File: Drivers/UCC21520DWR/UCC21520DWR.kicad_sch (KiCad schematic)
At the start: 21 parts, among them J1 Output, J3 Input, U1 UCC21520DWR

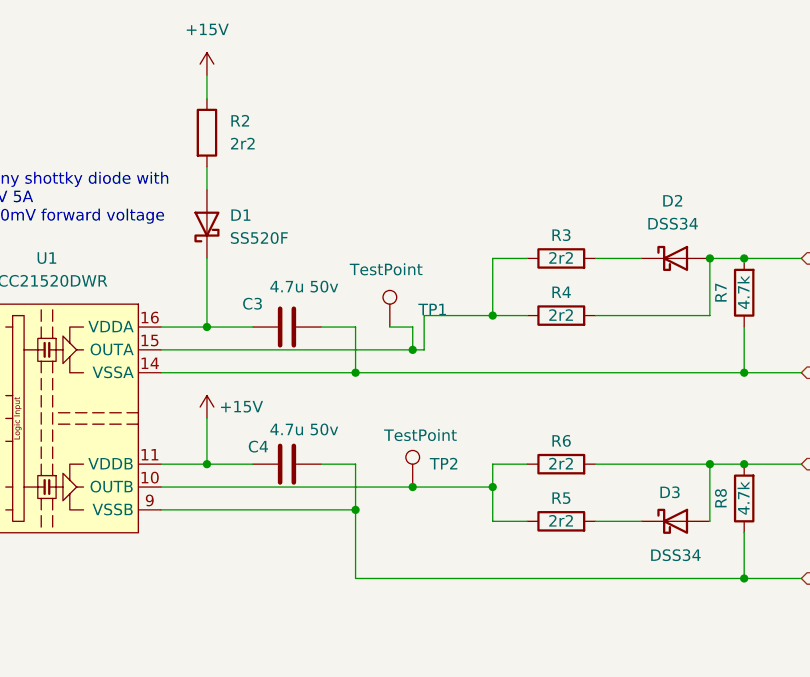
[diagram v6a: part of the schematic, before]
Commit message: fixes to caps and resistors on UCC21520DWR
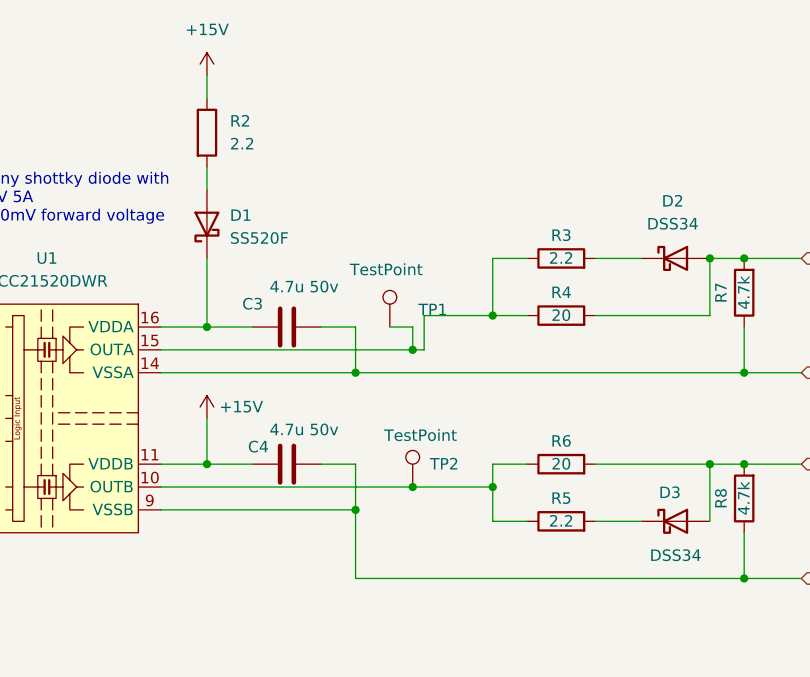
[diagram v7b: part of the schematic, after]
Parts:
- R2, R3, R5: value 2r2 -> 2.2
- R4, R6: value 2r2 -> 20; MPN C17521 -> C17544
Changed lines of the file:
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@@
       (effects (font (size 1.27 1.27)))
     )
-    (property "Value" "2r2" (at 196.85 90.17 90)
+    (property "Value" "20" (at 196.85 90.17 90)
       (effects (font (size 1.27 1.27)))
     )
@@
       (effects (font (size 1.27 1.27)) hide)
     )
-    (property "MPN" "C17521" (at 196.85 90.17 0)
+    (property "MPN" "C17544" (at 196.85 90.17 0)
       (effects (font (size 1.27 1.27)) hide)
     )
@@
       (effects (font (size 1.27 1.27)))
     )
-    (property "Value" "2r2" (at 196.85 106.68 90)
+    (property "Value" "20" (at 196.85 106.68 90)
       (effects (font (size 1.27 1.27)))
     )
@@
       (effects (font (size 1.27 1.27)) hide)
     )
-    (property "MPN" "C17521" (at 196.85 106.68 0)
+    (property "MPN" "C17544" (at 196.85 106.68 0)
       (effects (font (size 1.27 1.27)) hide)
     )
@@
       (effects (font (size 1.27 1.27)))
     )
-    (property "Value" "2r2" (at 196.85 83.82 90)
+    (property "Value" "2.2" (at 196.85 83.82 90)
       (effects (font (size 1.27 1.27)))
     )
@@
       (effects (font (size 1.27 1.27)) (justify left))
     )
-    (property "Value" "2r2" (at 160.02 71.12 0)
+    (property "Value" "2.2" (at 160.02 71.12 0)
       (effects (font (size 1.27 1.27)) (justify left))
     )
@@
       (effects (font (size 1.27 1.27)))
     )
-    (property "Value" "2r2" (at 196.85 113.03 90)
-      (effects (font (size 1.27 1.27)))
-    )
+    (property "Value" "2.2" (at 196.85 113.03 90)
+      (effects (font (size 1.27 1.27)))
+    )
